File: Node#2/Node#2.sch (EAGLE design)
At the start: 94 parts, among them IC1 TSL25911FN, J1 68712414522, Q1 BC847ALT1SMD, Q2 SI1308EDL-T1-GE3, U2 RV8564C3, U4 TPS63001DRCT

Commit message: Layout von Node#2 fertiggestellt
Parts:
- added ANT2: CONUFL001-SMD, BlueHome:CONUFL001-SMD
- added C53, C54, C55, C56, C57, C58, C59, C60, C61, C62: (no value), rcl:C-EUC0805K
- added C63, C64, C65, C66, C67, C68: (no value), rcl:C-EUC0805
- added C69, C70: (no value), rcl:C-EUC0402
- added D4: BAS40-06, diode:BAS40-06
- added JMP2: 0R-JUMPA, jump-0r-smd:0R-JUMPA
- added JP3: (no value), pinhead:PINHD-2X5
- added JP5: (no value), jumper:JP1E
- added JP7: (no value), pinhead:PINHD-1X3
- added JP8: (no value), pinhead:PINHD-1X2
- added R30, R31, R32, R33, R36, R37: (no value), rcl:R-EU_R0805
- added R34, R35: (no value), rcl:R-EU_R1210
- added S3, S4: FSM4JSMAATR, BlueHome:FSM4JSMAATR
- added U$13, U$15: L0402, BlueHome:L0402
- added U$14: BALF-NRG-01D3, BlueHome:BALF-NRG-01D3
- added U3: BLUENRG-232, BlueHome:BLUENRG-232
- added Y3: ECS-160-12-36-AGN-TR, BlueHome:ECS-160-12-36-AGN-TR
- added Y4: NX2012SA-32.768K-STD-MUB-1, BlueHome:NX2012SA-32.768K-STD-MUB-1
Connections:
- removed net MOSI: R3.1
- removed net RESET: U$2.RESETB
- removed net SCLK: R8.1
- new net DIO14: C68.1, JP8.1, R34.1, S4.1, S4.2, U3.DIO14/ANATEST0
- new net JTCK: JP3.4, U3.DIO9
- new net JTMS: JP3.2, U3.DIO10
- new net N$48: C59.1, C60.1, U3.VDD1V2
- new net N$49: C61.1, C62.1, JMP2-0R.2, U3.SMPSFILT1
- new net N$50: R31.1, S3.1, S3.2
- new net N$51: C64.1, U3.FXTAL1, Y3.OUT/IN
- new net N$52: C65.2, U3.FXTAL0, Y3.IN/OUT
- new net N$53: C66.2, C67.2, U$13.1
- new net N$54: C66.1, U3.SXTAL0, Y4.2
- new net N$55: C67.1, U3.SXTAL1, Y4.1
- new net N$56: C69.1, U$14.ANT, U$15.1
- new net N$57: ANT2.SIG, C70.1, U$15.2
- new net N$58: JP3.1, JP5.1
- new net N$59: JP8.2, R35.2, S4.3, S4.4
- new net N$60: U$14.RX_P, U3.RF1
- new net N$61: U$14.RX_N, U3.RF0
- new net RESETN: C63.2, D4.AA, JP3.10, R30.1, S3.3, S3.4, U$2.RESETB, U3.RESETN
- new net RXD: JP7.2, U3.DIO11
- new net SMPSFILT2: JMP2-0R.1, U3.SMPSFILT2
- new net TDI: JP3.8, R36.2, U3.DIO0
- new net TDO: JP3.6, R37.2, U3.DIO1
- new net TXD: JP7.1, U3.DIO8
- net +3V3: now also C53.1, C54.1, C55.1, C56.1, C57.1, C58.1, D4.K2, JMP2-0R.3, JP5.2, R30.2, R32.2, R33.2, R34.2, U3.VBAT1, U3.VBAT2, U3.VBAT3
- net ADC1: now also U3.ADC1
- net ADC2: now also U3.ADC2
- net DIO0: now also R36.1, R8.1
- net DIO1: now also R37.1
- net DIO12: now also U3.DIO12
- net DIO13: now also U3.DIO13
- net DIO2: now also R3.1, U3.DIO2
- net DIO3: now also U3.DIO3
- net DIO6: now also U3.DIO6
- net DIO7: now also U3.DIO7/BOOT
- net GND: now also ANT2.GND_1, ANT2.GND_2, C53.2, C54.2, C55.2, C56.2, C57.2, C58.2, C59.2, C60.2, C61.2, C62.2, C63.1, C64.2, C65.1, C68.2, C69.2, C70.2, JP3.3, JP3.5, JP3.9, JP7.3, R31.2, R35.1, U$13.2, U$14.GND, U3.EXP, U3.TEST, Y3.GND
- net SCL: now also R32.1, U3.DIO4
- net SDA: now also R33.1, U3.DIO5
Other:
- note added: "9 IO"
- note added: "ARM 10-PIN Interface"
- note added: "JTAG"
- note added: "Serial"

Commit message: Initial V2
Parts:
- removed ANT2: CONUFL001-SMD, BlueHome:CONUFL001-SMD
- removed C53, C54, C55, C56, C57, C58, C59, C60, C61, C62: (no value), rcl:C-EUC0805K
- removed C63, C64, C65, C66, C67, C68: (no value), rcl:C-EUC0805
- removed C69, C70: (no value), rcl:C-EUC0402
- removed D4: BAS40-06, diode:BAS40-06
- removed JMP2: 0R-JUMPA, jump-0r-smd:0R-JUMPA
- removed JP3: (no value), pinhead:PINHD-2X5
- removed JP5: (no value), jumper:JP1E
- removed JP7: (no value), pinhead:PINHD-1X3
- removed JP8: (no value), pinhead:PINHD-1X2
- removed R30, R31, R32, R33, R36, R37: (no value), rcl:R-EU_R0805
- removed R34, R35: (no value), rcl:R-EU_R1210
- removed S3, S4: FSM4JSMAATR, BlueHome:FSM4JSMAATR
- removed U$13, U$15: L0402, BlueHome:L0402
- removed U$14: BALF-NRG-01D3, BlueHome:BALF-NRG-01D3
- removed U3: BLUENRG-232, BlueHome:BLUENRG-232
- removed Y3: ECS-160-12-36-AGN-TR, BlueHome:ECS-160-12-36-AGN-TR
- removed Y4: NX2012SA-32.768K-STD-MUB-1, BlueHome:NX2012SA-32.768K-STD-MUB-1
- R16: value 10k -> 0k
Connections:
- removed net CS: R1.1, R18.2
- removed net DIO14: C68.1, JP8.1, R34.1, S4.1, S4.2, U3.DIO14/ANATEST0
- removed net JTCK: JP3.4, U3.DIO9
- removed net JTMS: JP3.2, U3.DIO10
- removed net N$48: C59.1, C60.1, U3.VDD1V2
- removed net N$49: C61.1, C62.1, JMP2-0R.2, U3.SMPSFILT1
- removed net N$50: R31.1, S3.1, S3.2
- removed net N$51: C64.1, U3.FXTAL1, Y3.OUT/IN
- removed net N$52: C65.2, U3.FXTAL0, Y3.IN/OUT
- removed net N$53: C66.2, C67.2, U$13.1
- removed net N$54: C66.1, U3.SXTAL0, Y4.2
- removed net N$55: C67.1, U3.SXTAL1, Y4.1
- removed net N$56: C69.1, U$14.ANT, U$15.1
- removed net N$57: ANT2.SIG, C70.1, U$15.2
- removed net N$58: JP3.1, JP5.1
- removed net N$59: JP8.2, R35.2, S4.3, S4.4
- removed net N$60: U$14.RX_P, U3.RF1
- removed net N$61: U$14.RX_N, U3.RF0
- removed net RXD: JP7.2, U3.DIO11
- removed net SMPSFILT2: JMP2-0R.1, U3.SMPSFILT2
- removed net TDI: JP3.8, R36.2, U3.DIO0
- removed net TDO: JP3.6, R37.2, U3.DIO1
- removed net TXD: JP7.1, U3.DIO8
- net +3V3: no longer C53.1, C54.1, C55.1, C56.1, C57.1, C58.1, D4.K2, JMP2-0R.3, JP5.2, R30.2, R32.2, R33.2, R34.2, U3.VBAT1, U3.VBAT2, U3.VBAT3
- net ADC1: no longer U3.ADC1
- net ADC2: no longer U3.ADC2
- net DIO0: no longer R36.1
- net DIO1: now also R1.1, R18.2; no longer R37.1
- net DIO12: no longer U3.DIO12
- net DIO13: no longer U3.DIO13
- net DIO2: no longer U3.DIO2
- net DIO3: no longer U3.DIO3
- net DIO6: no longer U3.DIO6
- net DIO7: no longer U3.DIO7/BOOT
- net GND: no longer ANT2.GND_1, ANT2.GND_2, C53.2, C54.2, C55.2, C56.2, C57.2, C58.2, C59.2, C60.2, C61.2, C62.2, C63.1, C64.2, C65.1, C68.2, C69.2, C70.2, JP3.3, JP3.5, JP3.9, JP7.3, R31.2, R35.1, U$13.2, U$14.GND, U3.EXP, U3.TEST, Y3.GND
- net RESETN: no longer C63.2, D4.AA, JP3.10, R30.1, S3.3, S3.4, U3.RESETN
- net SCL: no longer R32.1, U3.DIO4
- net SDA: no longer R33.1, U3.DIO5
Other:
- note removed: "9 IO"
- note removed: "ARM 10-PIN Interface"
- note removed: "JTAG"
- note removed: "Serial"

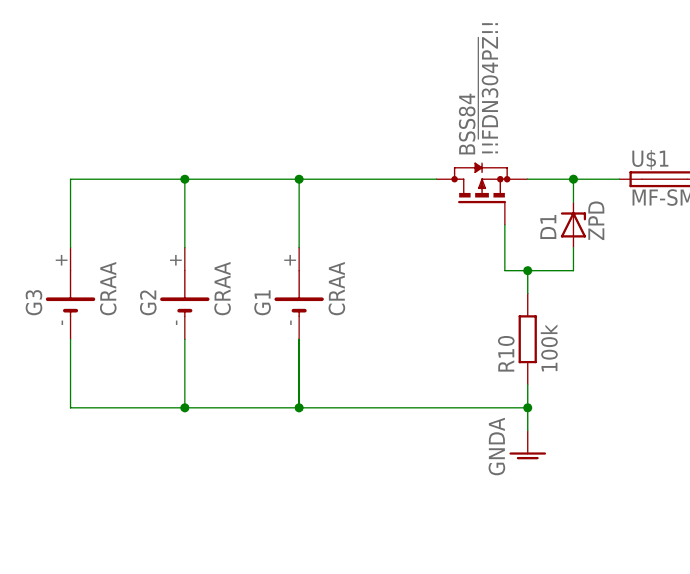
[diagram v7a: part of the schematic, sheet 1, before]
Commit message: Placed Buttons and Display
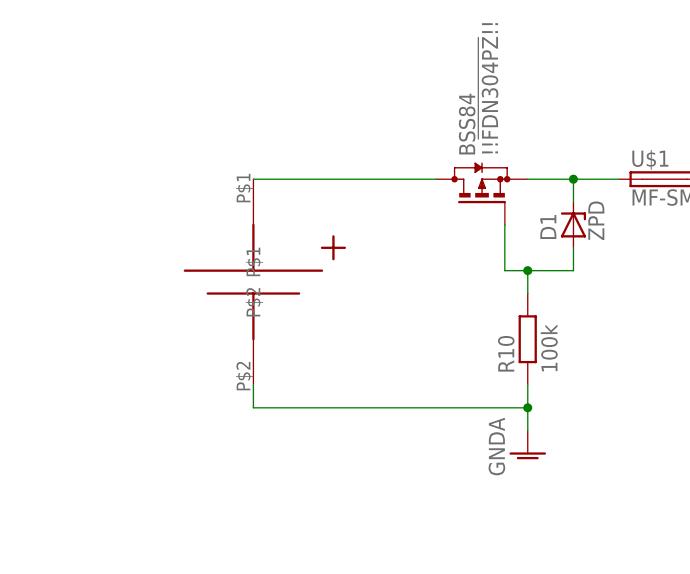
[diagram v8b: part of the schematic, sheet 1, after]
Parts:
- removed G1, G2, G3: CRAA, battery:CRAA
- added U$10: BATTER_HOLDER, BlueHome:BATTER_HOLDER
- added U$11: DISPLAY, BlueHome:DISPLAY
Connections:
- removed net N$15: G1.-, G2.-, G3.-
- net N$9: now also U$10.P$1; no longer G1.+, G2.+, G3.+
- net V-: now also U$10.P$2
